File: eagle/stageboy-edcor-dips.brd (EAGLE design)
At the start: 120 x 75 mm, 38 parts, among them IC1 MEGA8-P, IC2 7805TV, J2 DCJ0202, Q1 16MHz, X1 MIDI IN, X2 MIDI OUT, X4 22-23-2021, X6 GBIO

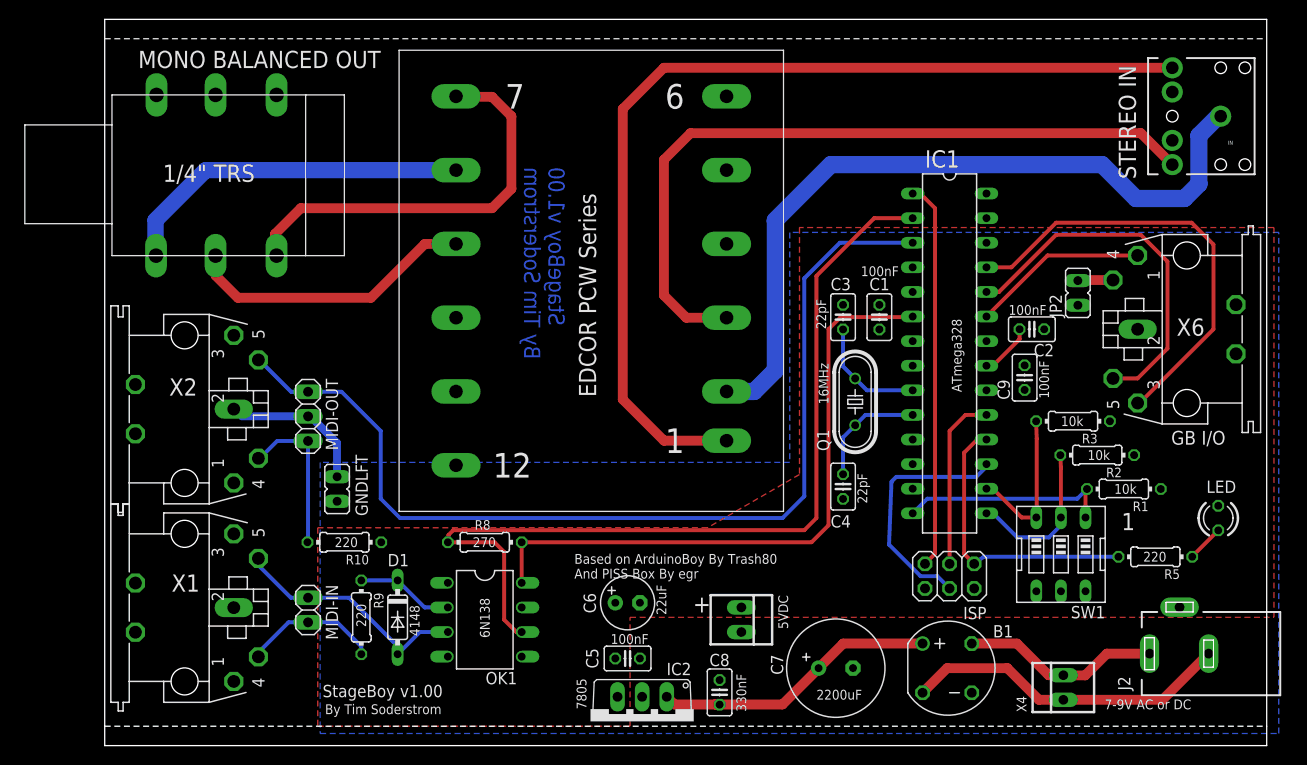
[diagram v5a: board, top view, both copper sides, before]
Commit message: Updated panels, board layout
Updated panels and boards to match each other and make sure things look
decent. Also formatting things for OshPark.
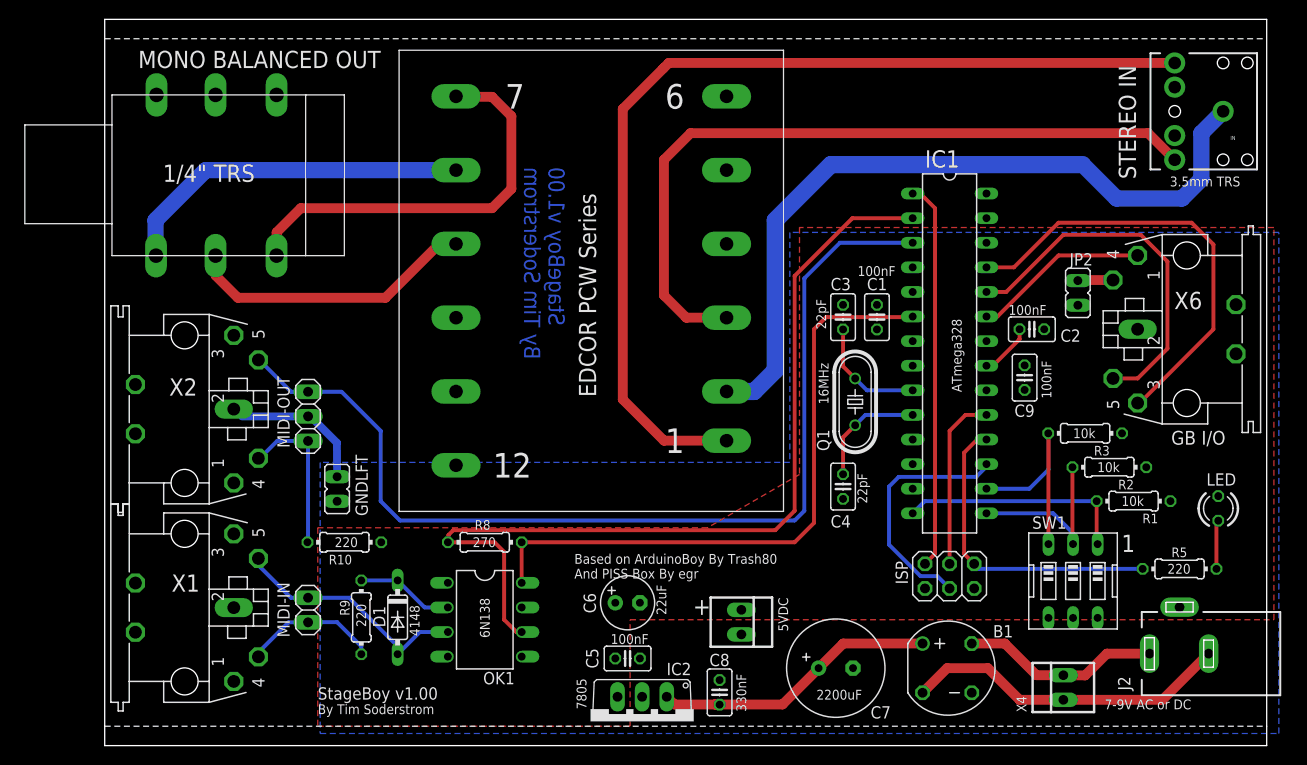
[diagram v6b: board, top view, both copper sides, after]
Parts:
- moved SW1 3.02 mm to (100.0, 17.0)
- moved R5 2.80 mm to (111.0, 18.2)
- moved R2 1.77 mm to (103.8, 28.8)
- moved R3 1.77 mm to (101.2, 32.2)
- moved R1 1.60 mm to (106.2, 25.2)
- moved LED 1.00 mm to (115.0, 24.5)
- moved IN 0.56 mm to (115.5, 65.5)
- moved 5VDC 0.25 mm to (65.8, 12.8)
- moved C1 0.25 mm to (79.8, 44.2)
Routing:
- net N$15: track 16.3 -> 22.4 mm
- net N$18: track 29.9 -> 32.4 mm
- net N$14: track 16.5 -> 18.9 mm
- net N$4: track 22.0 -> 24.1 mm
- net N$21: track 103.4 -> 104.6 mm
- net N$3: track 3.84 -> 5.06 mm
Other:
- board text added: "3.5mm TRS"

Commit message: Swapped out DC jack
Swapped DC jack out for one that uses large vias, as OshPark
doesn't do plated cutouts. Looks like most any DC jack will do,
but the part swapped was one from the SparkFun library.
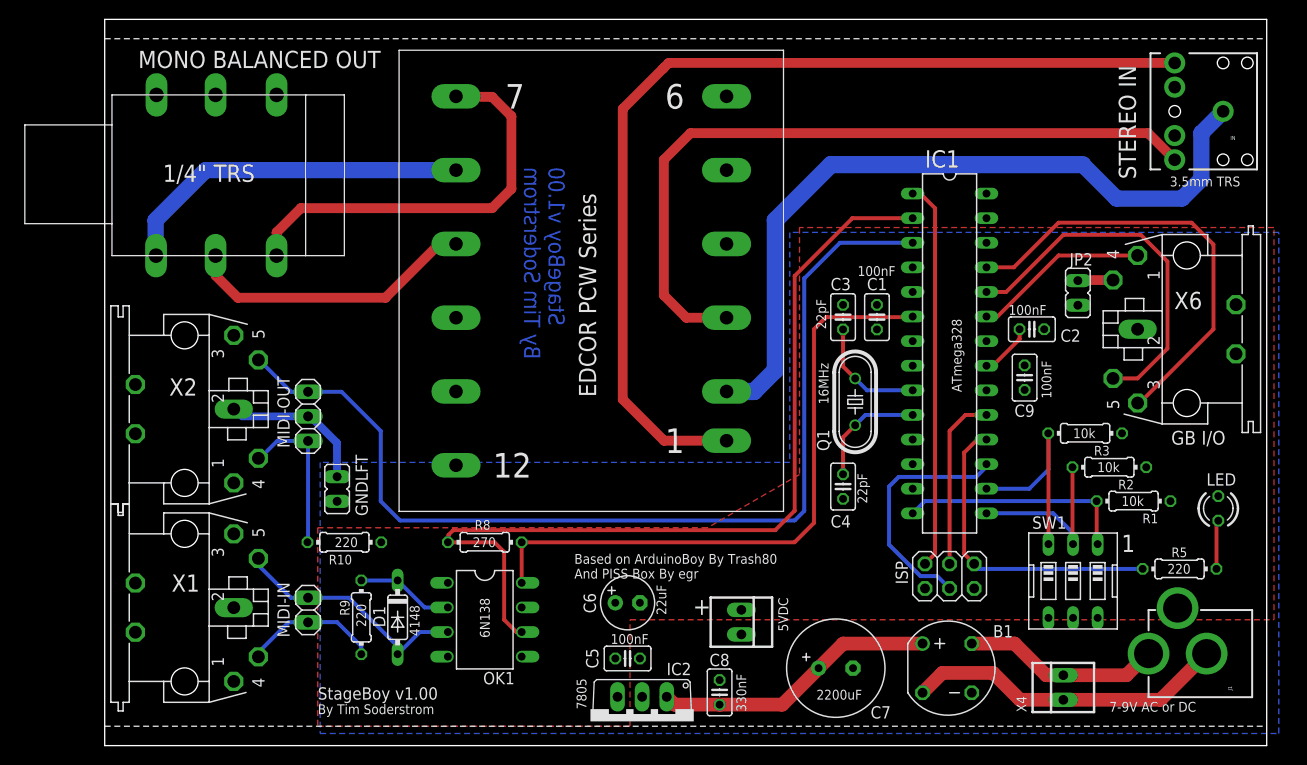
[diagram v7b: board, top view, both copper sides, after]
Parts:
- removed J2: DCJ0202, con-jack:DCJ0202
- added J1: POWER_JACKPTH, SparkFun-Connectors:POWER_JACK_PTH
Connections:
- net N$38: now also J1.GND; no longer J2.3
- net N$39: now also J1.PWR; no longer J2.1
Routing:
- net N$38: track 33.9 -> 33.3 mm
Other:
- outline, holes or cut-outs redrawn
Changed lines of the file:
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@@
 <layer number="106" name="bPlate" color="7" fill="1" visible="no" active="yes"/>
 <layer number="107" name="Crop" color="7" fill="1" visible="no" active="yes"/>
+<layer number="108" name="tplace-old" color="10" fill="1" visible="yes" active="yes"/>
+<layer number="109" name="ref-old" color="11" fill="1" visible="yes" active="yes"/>
 <layer number="116" name="Patch_BOT" color="9" fill="4" visible="no" active="yes"/>
 <layer number="121" name="_tsilk" color="7" fill="1" visible="no" active="yes"/>
@@
 <layer number="144" name="Drill_legend" color="7" fill="1" visible="no" active="yes"/>
 <layer number="151" name="HeatSink" color="7" fill="1" visible="no" active="yes"/>
+<layer number="199" name="Contour" color="7" fill="1" visible="yes" active="yes"/>
 <layer number="200" name="200bmp" color="1" fill="10" visible="no" active="yes"/>
 <layer number="201" name="201bmp" color="2" fill="10" visible="no" active="yes"/>
@@
 <plain>
 <wire x1="0" y1="0" x2="120" y2="0" width="0" layer="20"/>
-<wire x1="120" y1="0" x2="120" y2="2" width="0" layer="20"/>
-<wire x1="120" y1="2" x2="120" y2="75" width="0" layer="20"/>
+<wire x1="120" y1="0" x2="120" y2="75" width="0" layer="20"/>
 <wire x1="120" y1="75" x2="0" y2="75" width="0" layer="20"/>
-<wire x1="0" y1="75" x2="0" y2="2" width="0" layer="20"/>
-<wire x1="0" y1="2" x2="0" y2="0" width="0" layer="20"/>
+<wire x1="0" y1="75" x2="0" y2="0" width="0" layer="20"/>
 <wire x1="0" y1="2" x2="120" y2="2" width="0" layer="25" style="shortdash"/>
 <wire x1="0" y1="73" x2="120" y2="73" width="0" layer="25" style="shortdash"/>
@@
 <text x="77.75" y="48.5" size="1.016" layer="25">100nF</text>
 <text x="74.75" y="35.25" size="1.016" layer="25" rot="R90">16MHz</text>
-<text x="103.25" y="3.75" size="1.016" layer="25">7-9V AC or DC</text>
+<text x="103.75" y="3.5" size="1.016" layer="25">7-9V AC or DC</text>
 <text x="97.25" y="45.5" size="1.016" layer="25" rot="R180">100nF</text>
 <text x="96.75" y="39.75" size="1.016" layer="25" rot="R270">100nF</text>
@@
 <attribute name="OC_FARNELL" value="1462926" x="65.75" y="12.75" size="1.016" layer="27" rot="R270" display="off"/>
 </element>
-<element name="J2" library="con-jack" package="DCJ0202" value="DCJ0202" x="111" y="9.5" locked="yes" rot="R90">
-<attribute name="OC_NEWARK" value="unknown" x="111" y="9.5" size="1.778" layer="27" rot="R90" display="off"/>
-<attribute name="MPN" value="" x="111" y="9.5" size="1.778" layer="27" rot="R90" display="off"/>
-<attribute name="MF" value="" x="111" y="9.5" size="1.778" layer="27" rot="R90" display="off"/>
-<attribute name="OC_FARNELL" value="unknown" x="111" y="9.5" size="1.778" layer="27" rot="R90" display="off"/>
-</element>
+<element name="J1" library="SparkFun-Connectors" package="POWER_JACK_PTH" value="POWER_JACKPTH" x="121.5" y="9.5" rot="R90"/>
 </elements>
 <signals>
@@
 <contactref element="C8" pad="1"/>
 <contactref element="B1" pad="+"/>
-<wire x1="84.46" y1="10.54" x2="76.262" y2="10.54" width="1.016" layer="1"/>
-<wire x1="76.262" y1="10.54" x2="73.722" y2="8" width="1.016" layer="1"/>
-<wire x1="73.722" y1="8" x2="73.722" y2="7.972" width="1.016" layer="1"/>
-<wire x1="73.722" y1="7.972" x2="70" y2="4.25" width="1.016" layer="1"/>
-<wire x1="70" y1="4.25" x2="63.02" y2="4.25" width="1.016" layer="1"/>
-<wire x1="63.02" y1="4.25" x2="63.5" y2="4.23" width="1.016" layer="1"/>
-<wire x1="63.02" y1="4.25" x2="58.83" y2="4.25" width="1.016" layer="1"/>
-<wire x1="58.83" y1="4.25" x2="58.04" y2="5.04" width="1.016" layer="1"/>
+<wire x1="84.46" y1="10.54" x2="76.262" y2="10.54" width="1.4224" layer="1"/>
+<wire x1="76.262" y1="10.54" x2="73.722" y2="8" width="1.4224" layer="1"/>
+<wire x1="73.722" y1="8" x2="73.722" y2="7.972" width="1.4224" layer="1"/>
+<wire x1="73.722" y1="7.972" x2="69.98" y2="4.23" width="1.4224" layer="1"/>
+<wire x1="63.5" y1="4.23" x2="69.98" y2="4.23" width="1.4224" layer="1"/>
+<wire x1="63.5" y1="4.23" x2="58.85" y2="4.23" width="1.4224" layer="1"/>
+<wire x1="58.85" y1="4.23" x2="58.04" y2="5.04" width="1.4224" layer="1"/>
 </signal>
 <signal name="N$38">
 <contactref element="B1" pad="AC2"/>
 <contactref element="X4" pad="1"/>
-<wire x1="99" y1="4.73" x2="94.48" y2="4.73" width="1.016" layer="1"/>
-<wire x1="99" y1="4.73" x2="109.23" y2="4.73" width="1.016" layer="1"/>
-<contactref element="J2" pad="3"/>
-<wire x1="109.23" y1="4.73" x2="114" y2="9.5" width="1.016" layer="1"/>
-<wire x1="84.46" y1="5.46" x2="87" y2="8" width="1.016" layer="1"/>
-<wire x1="87" y1="8" x2="91.21" y2="8" width="1.016" layer="1"/>
-<wire x1="91.21" y1="8" x2="94.48" y2="4.73" width="1.016" layer="1"/>
+<contactref element="J1" pad="GND"/>
+<wire x1="99" y1="4.73" x2="109.03" y2="4.73" width="1.4224" layer="1"/>
+<wire x1="109.03" y1="4.73" x2="113.8" y2="9.5" width="1.4224" layer="1"/>
+<wire x1="99" y1="4.73" x2="94.52" y2="4.73" width="1.4224" layer="1"/>
+<wire x1="94.52" y1="4.73" x2="91.75" y2="7.5" width="1.4224" layer="1"/>
+<wire x1="91.75" y1="7.5" x2="86.5" y2="7.5" width="1.4224" layer="1"/>
+<wire x1="86.5" y1="7.5" x2="84.46" y2="5.46" width="1.4224" layer="1"/>
 </signal>
 <signal name="N$39">
 <contactref element="B1" pad="AC1"/>
 <contactref element="X4" pad="2"/>
-<wire x1="103.5" y1="9.5" x2="101.25" y2="7.25" width="1.016" layer="1"/>
-<wire x1="101.25" y1="7.25" x2="99.02" y2="7.25" width="1.016" layer="1"/>
-<wire x1="99.02" y1="7.25" x2="99" y2="7.27" width="1.016" layer="1"/>
-<contactref element="J2" pad="1"/>
-<wire x1="103.5" y1="9.5" x2="107.9" y2="9.5" width="1.016" layer="1"/>
-<wire x1="99" y1="7.27" x2="96.23" y2="7.27" width="1.016" layer="1"/>
-<wire x1="96.23" y1="7.27" x2="92.96" y2="10.54" width="1.016" layer="1"/>
-<wire x1="89.54" y1="10.54" x2="92.96" y2="10.54" width="1.016" layer="1"/>
+<contactref element="J1" pad="PWR"/>
+<wire x1="107.8" y1="9.5" x2="107.75" y2="9.5" width="1.4224" layer="1"/>
+<wire x1="107.75" y1="9.5" x2="105.52" y2="7.27" width="1.4224" layer="1"/>
+<wire x1="99" y1="7.27" x2="105.52" y2="7.27" width="1.4224" layer="1"/>
+<wire x1="99" y1="7.27" x2="97.23" y2="7.27" width="1.4224" layer="1"/>
+<wire x1="97.23" y1="7.27" x2="93.96" y2="10.54" width="1.4224" layer="1"/>
+<wire x1="89.54" y1="10.54" x2="93.96" y2="10.54" width="1.4224" layer="1"/>
 </signal>
 <signal name="N$43">

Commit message: Moved I/O components to the edges
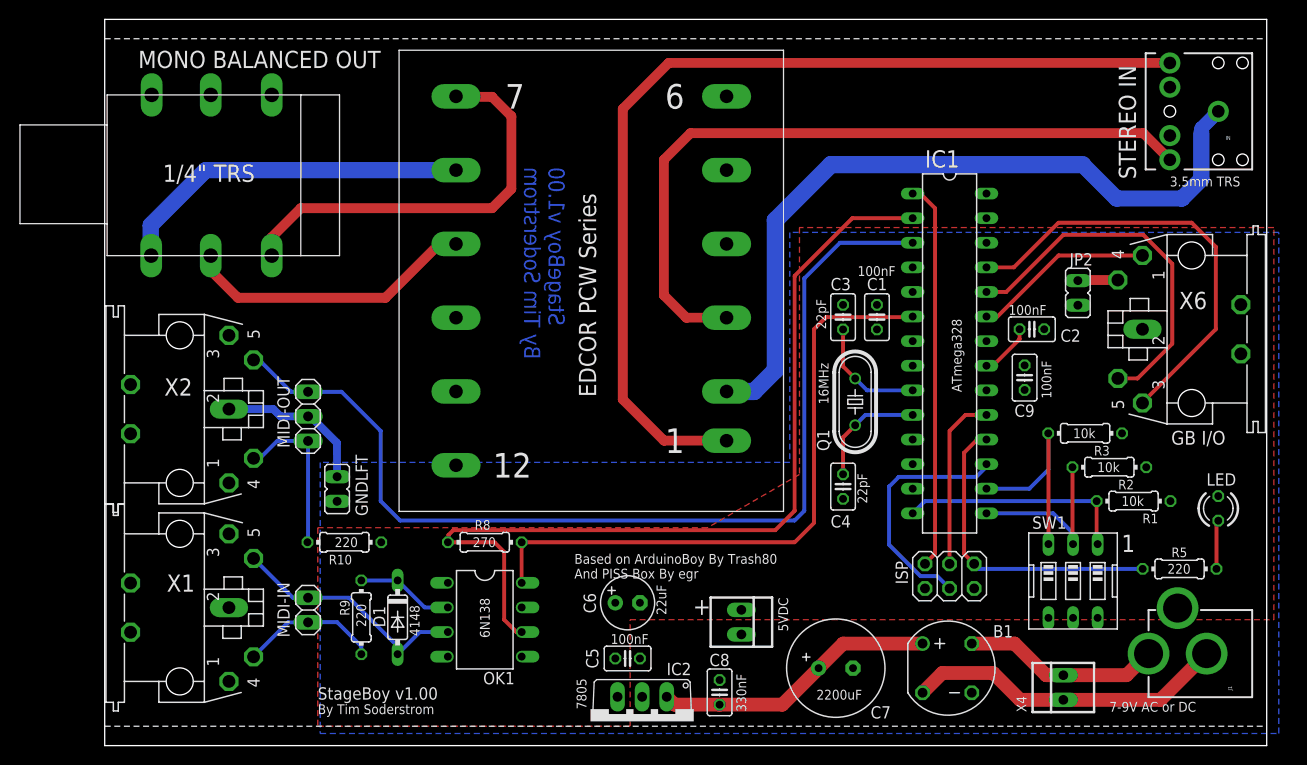
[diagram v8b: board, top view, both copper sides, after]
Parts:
- moved IN 0.50 mm to (115.0, 65.5)
- moved OUT 0.50 mm to (24.2, 59.0)
- moved X1 0.50 mm to (7.75, 14.2)
- moved X2 0.50 mm to (7.75, 34.8)
- moved X6 0.50 mm to (112.2, 43.0)
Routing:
- net N$43: track 14.4 -> 16.1 mm
- net N$29: track 101.5 -> 101.0 mm
- net N$20: track 3.65 -> 4.15 mm
- net N$40: track 76.5 -> 76.0 mm
- net N$27: track 16.4 -> 16.9 mm
- net N$26: track 18.2 -> 18.7 mm
- net N$21: track 104.6 -> 105.1 mm
